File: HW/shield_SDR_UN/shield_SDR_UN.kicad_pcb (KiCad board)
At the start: 2 copper layers, 100 x 100 mm, 227 parts, among them J1 Conn_02x09_Odd_Even, J2 Conn_02x08_Odd_Even, J3 Conn_02x10_Top_Bottom, J4 USB_B_Micro, J5 USB_A, J6 Conn_02x06_Odd_Even, J7 Conn_01x03_Male, P1 GSG-RF-CONN, P2 GSG-RF-CONN, Q1 MOSFET_P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

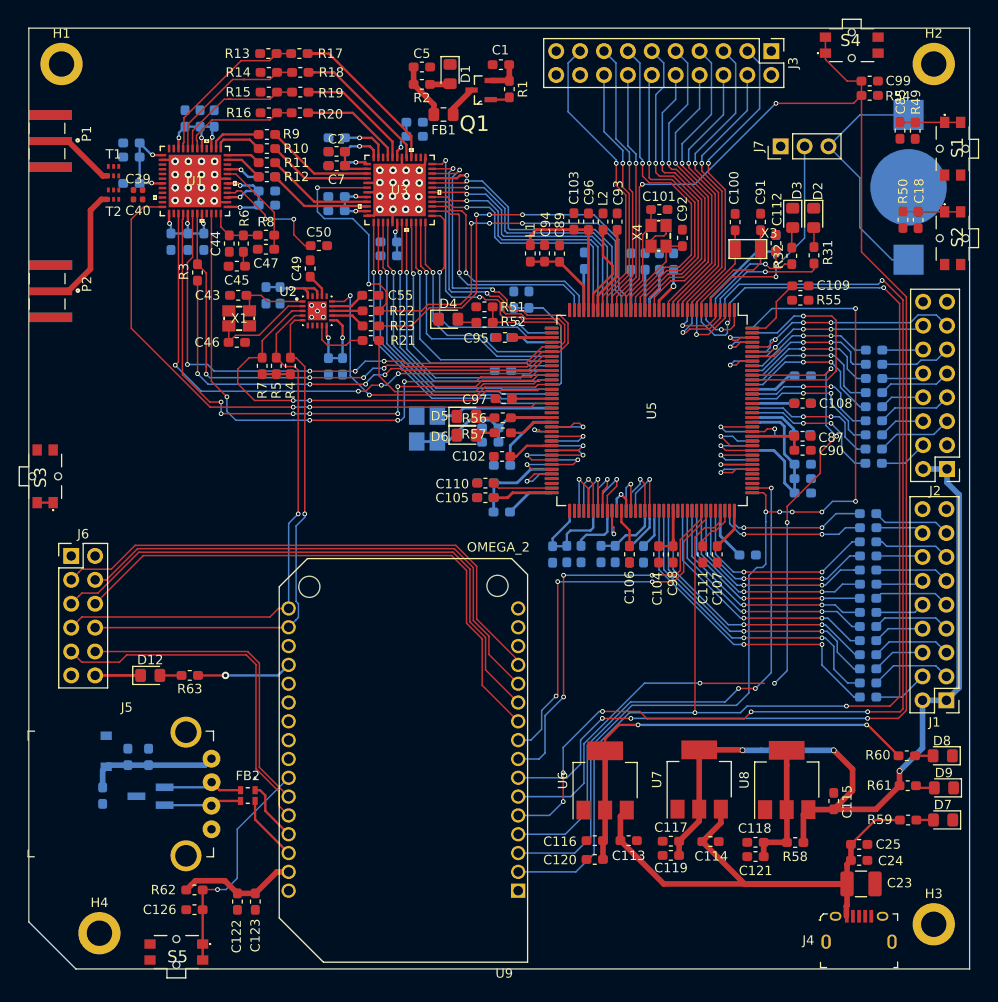
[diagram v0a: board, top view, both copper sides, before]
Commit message: Switchs modified
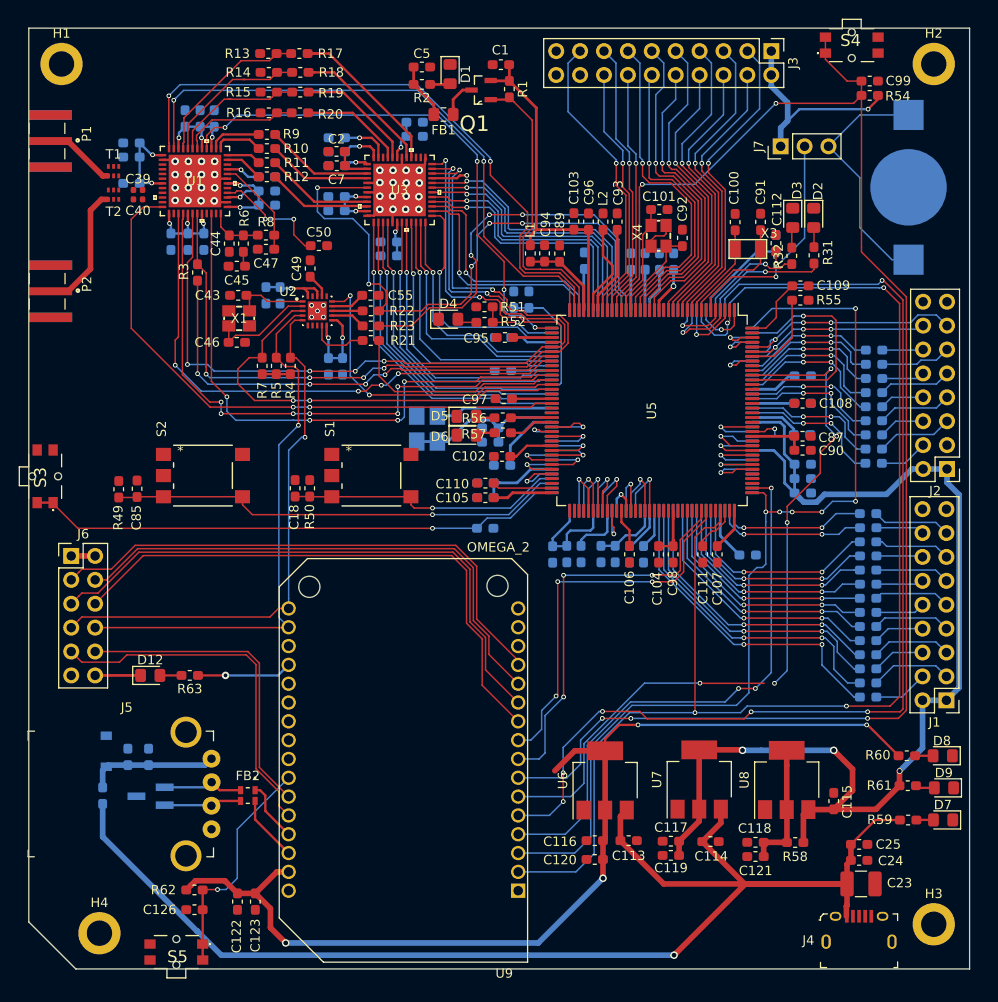
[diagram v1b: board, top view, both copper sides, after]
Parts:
- S1, S2: value TL1014BF160QG -> FSM1LPTR; footprint lib:TL1014BF160QG -> lib:FSM1LPTR
- moved R49 92.8 mm to (75.0, 87.0), turned to 90 degrees
- moved C85 89.6 mm to (77.0, 87.0), turned to 90 degrees
- moved S2 87.5 mm to (79.8, 83.3), turned to 180 degrees
- moved S1 74.1 mm to (97.7, 83.3), turned to 180 degrees
- moved C18 72.1 mm to (93.8, 87.0), turned to 90 degrees
- moved R50 69.2 mm to (95.3, 87.0), turned to 90 degrees
- moved R53 2.47 mm to (114.0, 91.2), turned to 180 degrees
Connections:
- net /FPGA/FPGA_JTDO renamed /FPGA_JTDO
- net /omega_2/BOOT_0 renamed /BOOT_0
- net /omega_2/OMG_JNRST renamed /OMG_JNRST
- net /omega_2/OMG_JTCK renamed /OMG_JTCK
- net /omega_2/OMG_JTDI renamed /OMG_JTDI
- net /omega_2/OMG_JTMS renamed /OMG_JTMS
- net /omega_2/OMG_JTRST renamed /OMG_JTRST
- net /proc/STM_JTDO renamed /STM_JTDO
- S1 pad 1: /FPGA/BTN1 -> /FPGA/BTN2
- S1 pad 2: /FPGA/BTN1 -> /FPGA/BTN2
- S1 pad 4: 3V3 FPGA -> Net-(S1-Pad4)
- S1 pad 5: (no net) -> Net-(S1-Pad4)
- S2 pad 1: /FPGA/BTN2 -> /FPGA/BTN1
- S2 pad 2: /FPGA/BTN2 -> /FPGA/BTN1
- S2 pad 4: 3V3 FPGA -> Net-(S2-Pad4)
- S2 pad 5: (no net) -> Net-(S2-Pad4)
- U4 pad 39: /FPGA/BTN2 -> /FPGA/BTN1
- U4 pad 40: /FPGA/BTN1 -> /FPGA/BTN2
- U5 pad 35: rf_ANTSEL -> rf_RXTX
- U5 pad 36: rf_RXHP -> rf_ANTSEL
- U5 pad 37: rf_RXTX -> rf_RXHP
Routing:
- net 3V3 MCU: track 167.2 -> 260.3 mm, vias 7 -> 10
- net +5V: track 65.4 -> 156.4 mm, vias 0 -> 1
- net rf_RXTX: track 0.00 -> 66.2 mm, vias 0 -> 2
- net rf_ANTSEL: track 0.00 -> 63.7 mm, vias 0 -> 2
- net rf_RXHP: track 0.00 -> 56.3 mm, vias 0 -> 4
- net /FPGA/PROGRAM_B: track 6.98 -> 57.4 mm, vias 0 -> 1
- net /FPGA/BTN1: track 6.46 -> 48.8 mm, vias 0 -> 1
- net !VAA_ENABLE: track 2.08 -> 30.7 mm
- net /FPGA/BTN2: track 6.14 -> 29.6 mm, vias 0 -> 1
- net 3V3 FPGA: track 224.3 -> 238.3 mm
- net /BOOT_0: track 3.31 -> 9.08 mm
- net I2C_SCL: track 78.5 -> 80.4 mm
- net GCK0: track 65.9 -> 64.7 mm
- net I2C_SDA: track 84.7 -> 83.7 mm
- net Net-(FB1-Pad1): track 3.41 -> 3.97 mm

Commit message: PCB_rout_1
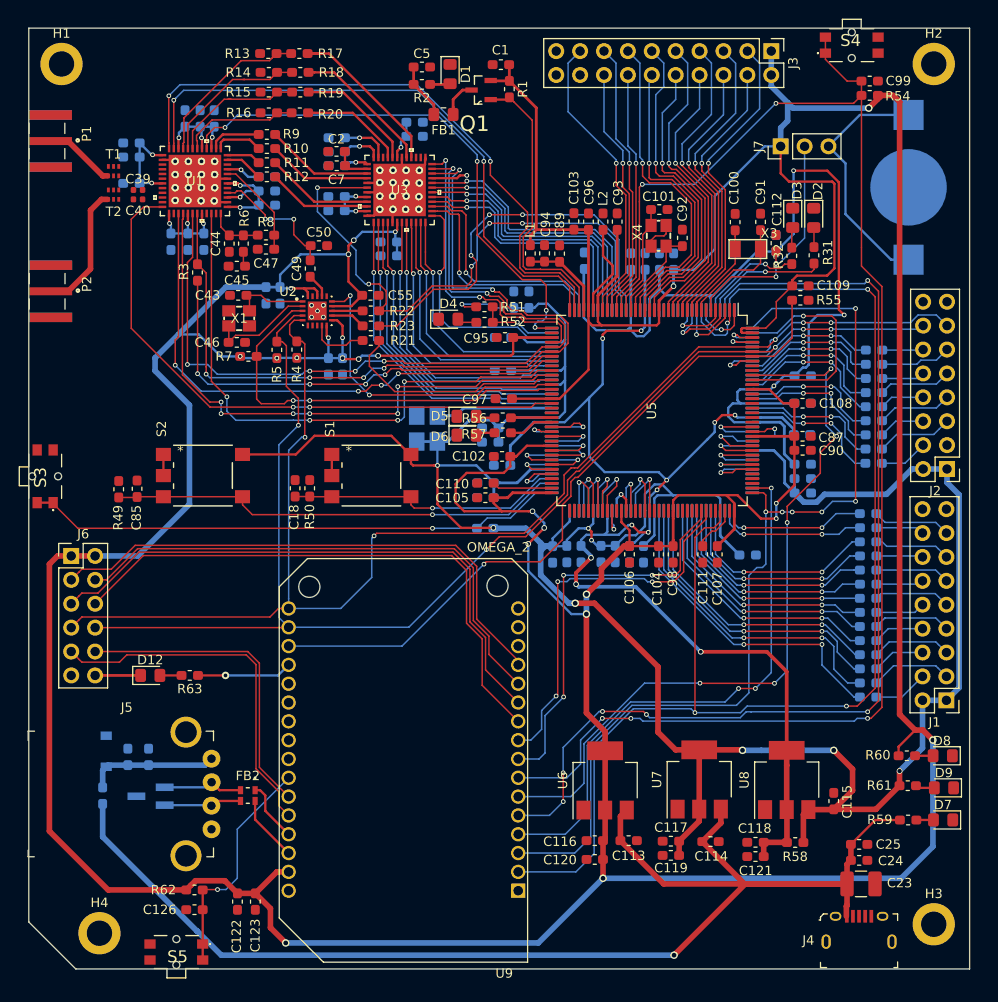
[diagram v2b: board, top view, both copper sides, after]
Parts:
- moved R4 1.86 mm to (93.9, 72.2)
- moved R7 1.78 mm to (88.8, 72.9), turned to 0 degrees
- moved R5 1.71 mm to (91.8, 72.2)
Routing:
- net 3V3 MCU: track 260.3 -> 654.9 mm, vias 10 -> 24
- net 3V3 FPGA: track 238.3 -> 422.0 mm, vias 3 -> 12
- net 1V2 FPGA: track 41.9 -> 138.9 mm, vias 0 -> 11
- net /BOOT_0: track 9.08 -> 74.2 mm, vias 0 -> 1
- net I2C_SDA: track 83.7 -> 148.2 mm, vias 4 -> 5
- net I2C_SCL: track 80.4 -> 142.4 mm, vias 4 -> 5
- net /FPGA_JTDO: track 114.9 -> 109.6 mm
- net /OMG_JTMS: track 140.0 -> 135.2 mm
- net /OMG_JNRST: track 163.2 -> 159.6 mm
- net GPIO_INTR: track 46.7 -> 44.3 mm
- net GCK0: track 64.7 -> 62.4 mm
- net Net-(S2-Pad4): track 0.00 -> 2.25 mm
- net Net-(S1-Pad4): track 0.00 -> 2.25 mm
- net /rf_front_end/XTAL: track 12.6 -> 14.1 mm
- net rf_RXHP: track 56.3 -> 57.9 mm
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
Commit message: PCB_rout_2
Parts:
- turned C39 to 180 degrees
- turned C40 to 180 degrees
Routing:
- net GND: track 44.7 -> 246.6 mm, vias 37 -> 205
- net VAA: track 67.3 -> 179.0 mm, vias 15 -> 19
- net Net-(T1-Pad4): track 0.00 -> 4.77 mm
- net Net-(T1-Pad3): track 0.00 -> 4.73 mm
- net FMC_D0: track 3.89 -> 8.48 mm
- net 3V3 FPGA: track 422.0 -> 424.6 mm
- net Net-(C39-Pad1): track 0.00 -> 2.24 mm
- net Net-(C40-Pad1): track 0.00 -> 2.20 mm
- net Net-(C40-Pad2): track 0.00 -> 1.57 mm
- net Net-(C39-Pad2): track 0.00 -> 1.57 mm
- net /FPGA/CLK80MHz: track 12.5 -> 13.7 mm
- net adDD6: track 28.9 -> 28.2 mm
- net adDA6: track 28.8 -> 28.3 mm
- added copper zone on B.Cu, net GND
- added copper zone on F.Cu, net GND

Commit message: PCB routing
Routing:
- net GND: vias 205 -> 201
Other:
- rule trace_min: 0.16 -> 0.153
- board text removed: "Profe vea esta belleza, pongame 5"

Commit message: PCB routing
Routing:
- net GND: vias 201 -> 218
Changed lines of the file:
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@@
     (thickness 1.6)
     (drawings 7)
-    (tracks 3058)
+    (tracks 3075)
     (modules 227)
     (nets 310)
@@
       (effects (font (size 1.00002 1.00002) (thickness 0.05)))
     )
-    (fp_text value "OMEGA_2" (at -10.0938 22.6573) (layer "F.SilkS")
+    (fp_text value "OMEGA_2" (at -0.24 22.6573) (layer "F.SilkS")
       (effects (font (size 1.00187 1.00187) (thickness 0.05)))
     )
@@
     (tags "capacitor")
     (attr smd)
-    (fp_text reference "C39" (at 0.22 1.07) (layer "F.SilkS")
+    (fp_text reference "C39" (at 0.05 1.07) (layer "F.SilkS")
       (effects (font (size 1 1) (thickness 0.15)))
     )
@@
   (module "lib:MAX5864ETM&plus_" (layer "F.Cu")
     (at 104.85 55.24)
-    (fp_text reference "U3" (at 0 0) (layer "F.SilkS")
+    (fp_text reference "U3" (at -2.35 -5.24) (layer "F.SilkS")
       (effects (font (size 1 1) (thickness 0.15)))
     )
@@
   (module "lib:MAX2830ETM&plus_" (layer "F.Cu")
     (at 83.1 54.29)
-    (fp_text reference "U1" (at 0 0) (layer "F.SilkS")
+    (fp_text reference "U1" (at -4.1 -4.79) (layer "F.SilkS")
       (effects (font (size 1 1) (thickness 0.15)))
     )
@@
     (at 113.52 44.62 180)
     (attr smd)
-    (fp_text reference "Q1" (at 0.7113 -3.58193) (layer "F.SilkS")
-      (effects (font (size 1.64024 1.64024) (thickness 0.05)))
+    (fp_text reference "Q1" (at 0.02 -2.38) (layer "F.SilkS")
+      (effects (font (size 1 1) (thickness 0.15)))
     )
     (fp_text value "MOSFET_P" (at 1.75268 3.40373) (layer "F.SilkS") hide
@@
     (tags "mounting hole 2.7mm m2.5 iso14580")
     (attr virtual)
-    (fp_text reference "H2" (at 0 -3.25) (layer "F.SilkS")
+    (fp_text reference "H2" (at 0 3.65) (layer "F.SilkS")
       (effects (font (size 1 1) (thickness 0.15)))
     )
@@
     (descr "TL1014B")
     (tags "Switch")
-    (fp_text reference "S4" (at 0 0) (layer "F.SilkS")
+    (fp_text reference "S4" (at 1.79 -3.652) (layer "F.SilkS")
       (effects (font (size 1.27 1.27) (thickness 0.254)))
     )
@@
     (tags "resistor handsolder")
     (attr smd)
-    (fp_text reference "R57" (at 3.065 -0.14) (layer "F.SilkS")
-      (effects (font (size 1 1) (thickness 0.15)))
+    (fp_text reference "R57" (at -2.683 0.054) (layer "F.SilkS")
+      (effects (font (size 0.5 0.5) (thickness 0.1)))
     )
     (fp_text value "470" (at 0 1.43) (layer "F.Fab")
@@
     (tags "resistor handsolder")
     (attr smd)
-    (fp_text reference "R56" (at 3.025 -0.05) (layer "F.SilkS")
-      (effects (font (size 1 1) (thickness 0.15)))
+    (fp_text reference "R56" (at -2.683 -0.046) (layer "F.SilkS")
+      (effects (font (size 0.5 0.5) (thickness 0.1)))
     )
     (fp_text value "470" (at 0 1.43) (layer "F.Fab")
@@
   (via (at 104.394 59.69) (size 0.5) (drill 0.3) (layers "F.Cu" "B.Cu") (net 1))
   (via (at 148.32 66.9) (size 0.6) (drill 0.4) (layers "F.Cu" "B.Cu") (net 2))
-  (via (at 130.14 124.32) (size 0.8) (drill 0.5) (layers "F.Cu" "B.Cu") (net 2))
   (via (at 113.11 86.32) (size 0.5) (drill 0.3) (layers "F.Cu" "B.Cu") (net 2))
   (via (at 113.09 87.92) (size 0.5) (drill 0.3) (layers "F.Cu" "B.Cu") (net 2))
@@
   (via (at 86.81 134.74) (size 0.8) (drill 0.5) (layers "F.Cu" "B.Cu") (net 2))
   (via (at 89.49 134.76) (size 0.8) (drill 0.5) (layers "F.Cu" "B.Cu") (net 2))
-  (via (at 130.01 115.12) (size 0.8) (drill 0.5) (layers "F.Cu" "B.Cu") (net 2))
-  (via (at 132.07 115.37) (size 0.8) (drill 0.5) (layers "F.Cu" "B.Cu") (net 2))
-  (via (at 130.34 117.18) (size 0.8) (drill 0.5) (layers "F.Cu" "B.Cu") (net 2))
-  (via (at 132.72 117.18) (size 0.8) (drill 0.5) (layers "F.Cu" "B.Cu") (net 2))
-  (via (at 131.63 118.41) (size 0.8) (drill 0.5) (layers "F.Cu" "B.Cu") (net 2))
-  (via (at 131.73 120.76) (size 0.8) (drill 0.5) (layers "F.Cu" "B.Cu") (net 2))
   (via (at 140.06 117.41) (size 0.8) (drill 0.5) (layers "F.Cu" "B.Cu") (net 2))
   (via (at 143.19 117.39) (size 0.8) (drill 0.5) (layers "F.Cu" "B.Cu") (net 2))
@@
   (via (at 142.76 54.77) (size 0.8) (drill 0.5) (layers "F.Cu" "B.Cu") (net 2))
   (via (at 144.83 54.76) (size 0.8) (drill 0.5) (layers "F.Cu" "B.Cu") (net 2))
-  (via (at 162.84 47.59) (size 0.8) (drill 0.5) (layers "F.Cu" "B.Cu") (net 2))
-  (via (at 163.11 49.93) (size 0.8) (drill 0.5) (layers "F.Cu" "B.Cu") (net 2))
-  (via (at 163.02 60.37) (size 0.8) (drill 0.5) (layers "F.Cu" "B.Cu") (net 2))
-  (via (at 163.02 63.28) (size 0.8) (drill 0.5) (layers "F.Cu" "B.Cu") (net 2))
   (via (at 124.62 45.82) (size 0.8) (drill 0.5) (layers "F.Cu" "B.Cu") (net 2))
   (segment (start 116.99 66.025) (end 116.99 66.01) (width 0.25) (layer "B.Cu") (net 2))
@@
   (segment (start 116.99 66.01) (end 116.99 66.01) (width 0.25) (layer "B.Cu") (net 2))
   (via (at 116.99 66.01) (size 0.5) (drill 0.3) (layers "F.Cu" "B.Cu") (net 2))
+  (via (at 128.5 99.5) (size 0.5) (drill 0.3) (layers "F.Cu" "B.Cu") (net 2))
+  (via (at 129.5 100.5) (size 0.5) (drill 0.3) (layers "F.Cu" "B.Cu") (net 2))
+  (via (at 130.5 101.5) (size 0.5) (drill 0.3) (layers "F.Cu" "B.Cu") (net 2))
+  (via (at 131.5 102.5) (size 0.5) (drill 0.3) (layers "F.Cu" "B.Cu") (net 2))
+  (via (at 132.5 103.5) (size 0.5) (drill 0.3) (layers "F.Cu" "B.Cu") (net 2))
+  (via (at 133.5 104.5) (size 0.5) (drill 0.3) (layers "F.Cu" "B.Cu") (net 2))
+  (via (at 134.5 105.5) (size 0.5) (drill 0.3) (layers "F.Cu" "B.Cu") (net 2))
+  (via (at 130 115) (size 0.5) (drill 0.3) (layers "F.Cu" "B.Cu") (net 2))
+  (via (at 132.5 115) (size 0.5) (drill 0.3) (layers "F.Cu" "B.Cu") (net 2))
+  (via (at 132.5 117.5) (size 0.5) (drill 0.3) (layers "F.Cu" "B.Cu") (net 2))
+  (via (at 130 117.5) (size 0.5) (drill 0.3) (layers "F.Cu" "B.Cu") (net 2))
+  (via (at 132 120) (size 0.5) (drill 0.3) (layers "F.Cu" "B.Cu") (net 2))
+  (via (at 132 122) (size 0.5) (drill 0.3) (layers "F.Cu" "B.Cu") (net 2))
+  (via (at 155 118) (size 0.5) (drill 0.3) (layers "F.Cu" "B.Cu") (net 2))
+  (via (at 155 116) (size 0.5) (drill 0.3) (layers "F.Cu" "B.Cu") (net 2))
+  (via (at 155 114) (size 0.5) (drill 0.3) (layers "F.Cu" "B.Cu") (net 2))
+  (via (at 163 112) (size 0.5) (drill 0.3) (layers "F.Cu" "B.Cu") (net 2))
+  (via (at 163 64) (size 0.6) (drill 0.4) (layers "F.Cu" "B.Cu") (net 2))
+  (via (at 163 61) (size 0.6) (drill 0.4) (layers "F.Cu" "B.Cu") (net 2))
+  (via (at 163 49) (size 0.6) (drill 0.4) (layers "F.Cu" "B.Cu") (net 2))
+  (via (at 163 46) (size 0.6) (drill 0.4) (layers "F.Cu" "B.Cu") (net 2))
+  (via (at 148 40) (size 0.6) (drill 0.4) (layers "F.Cu" "B.Cu") (net 2))
+  (via (at 148 43) (size 0.6) (drill 0.4) (layers "F.Cu" "B.Cu") (net 2))
+  (via (at 117 40) (size 0.6) (drill 0.4) (layers "F.Cu" "B.Cu") (net 2))
+  (via (at 115 40) (size 0.6) (drill 0.4) (layers "F.Cu" "B.Cu") (net 2))
+  (via (at 113 40) (size 0.6) (drill 0.4) (layers "F.Cu" "B.Cu") (net 2))
+  (via (at 111 40) (size 0.6) (drill 0.4) (layers "F.Cu" "B.Cu") (net 2))
+  (via (at 109 40) (size 0.6) (drill 0.4) (layers "F.Cu" "B.Cu") (net 2))
   (segment (start 86.562 54.55) (end 86.552 54.54) (width 0.25) (layer "F.Cu") (net 3))
   (segment (start 99.05 51.165) (end 99.025 51.14) (width 0.25) (layer "F.Cu") (net 3))

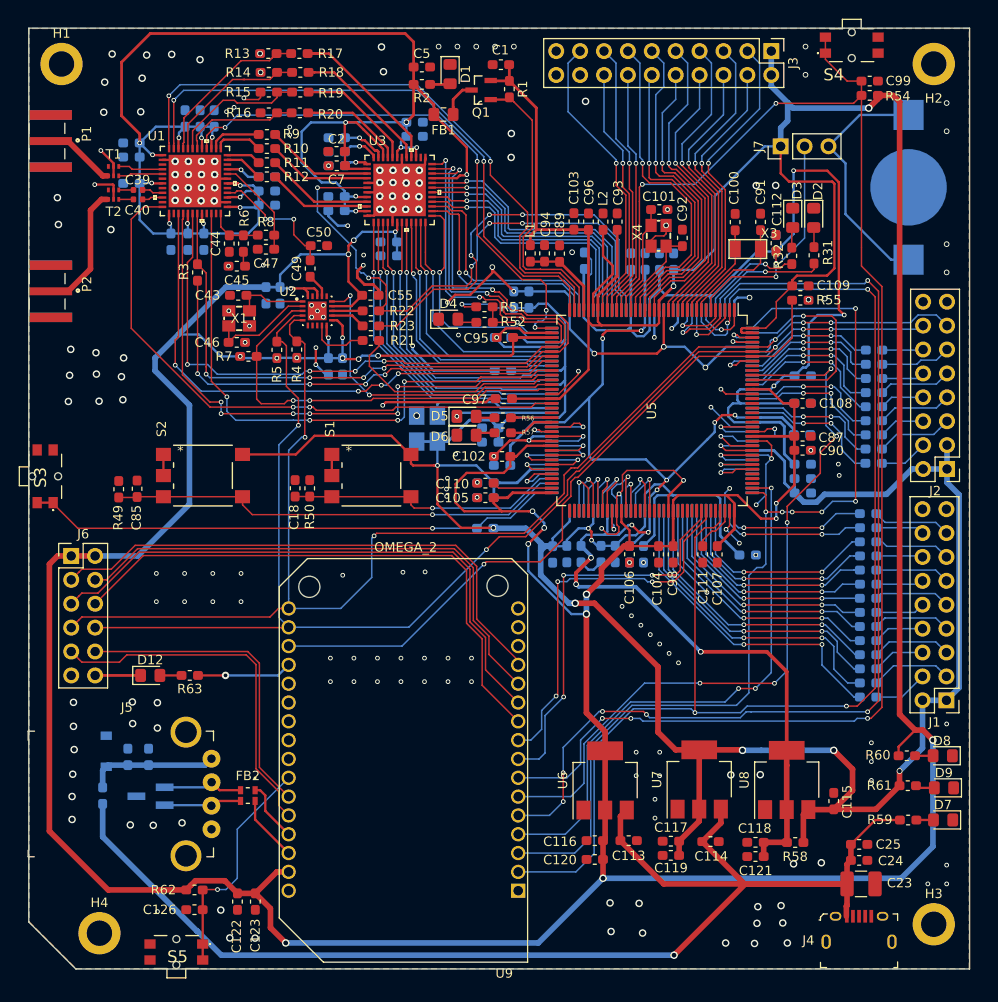
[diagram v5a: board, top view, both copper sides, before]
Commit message: design rules corrections
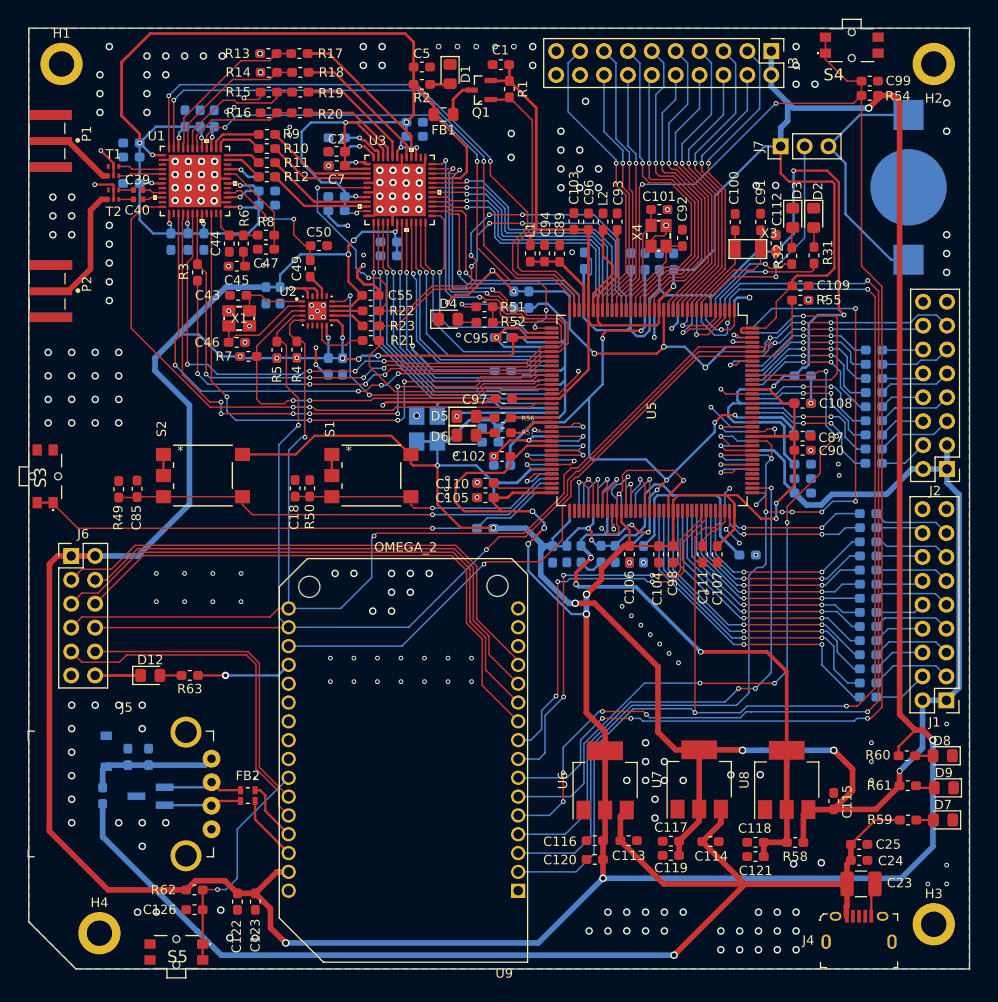
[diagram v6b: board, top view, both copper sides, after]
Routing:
- net GND: track 246.6 -> 252.3 mm, vias 218 -> 278
- net /OMG_JTRST: track 80.2 -> 79.1 mm
- net FMC_D10: track 5.77 -> 5.01 mm
- net rf_RXTX: track 66.2 -> 67.0 mm
- net rf_RXHP: track 57.9 -> 58.5 mm
- net /STM_JTDO: track 24.5 -> 25.0 mm
- net VAA: vias 19 -> 18

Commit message: PCB routing
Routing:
- net GND: track 252.3 -> 275.8 mm, vias 278 -> 277
- net 3V3 MCU: track 654.9 -> 663.0 mm
- net 3V3 FPGA: track 424.8 -> 426.3 mm
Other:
- rule trace_min: 0.153 -> 0.16
